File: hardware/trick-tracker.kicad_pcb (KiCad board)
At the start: 4 copper layers, 31 x 45 mm, 58 parts, among them J1 USB4105-GF-A, J2 S2B-PH-K, J3 QWiiC, J4 MEM2061-01-188-00-A, J6 QWiiC, P1 SMTB-1240-S-R, U1 MS88SF2, U2 DPS368XTSA1, U3 LSM9DS1, U4 MCP73831/OT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

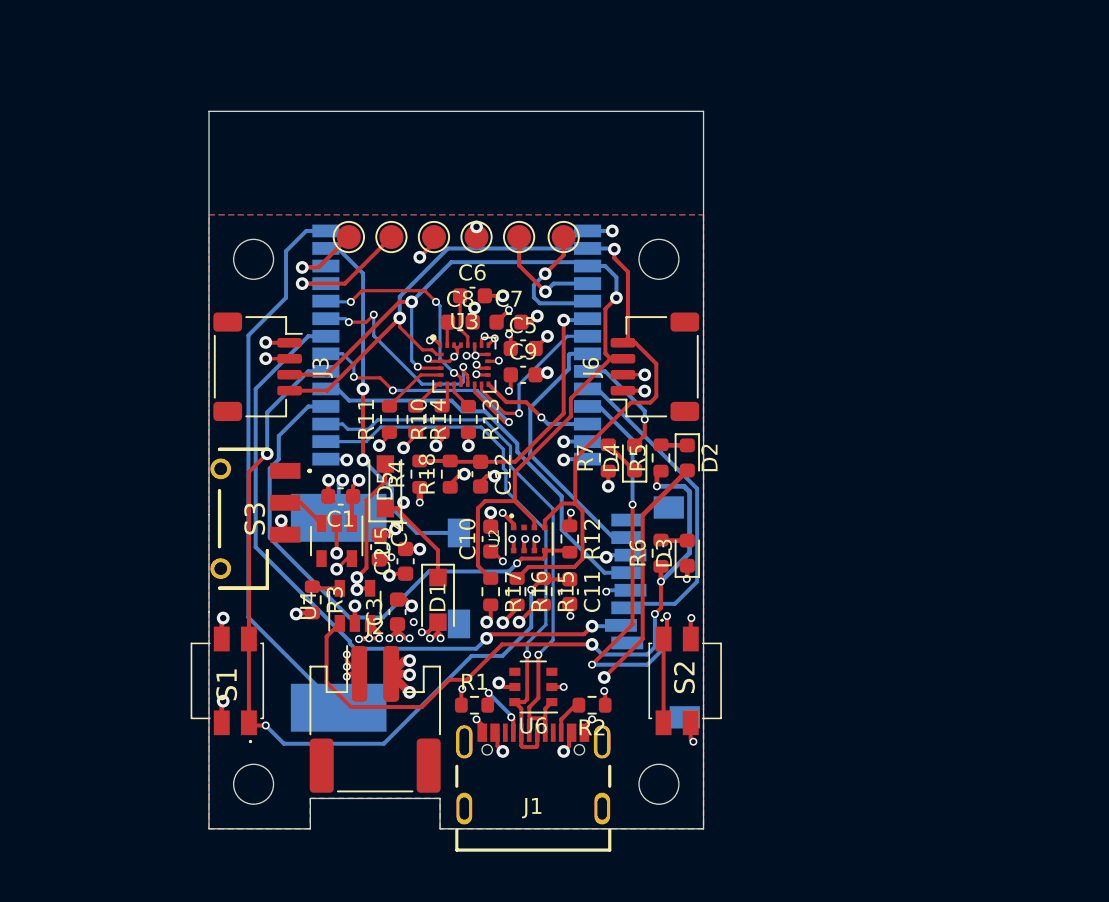
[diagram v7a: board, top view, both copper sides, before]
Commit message: Placed and moved labels
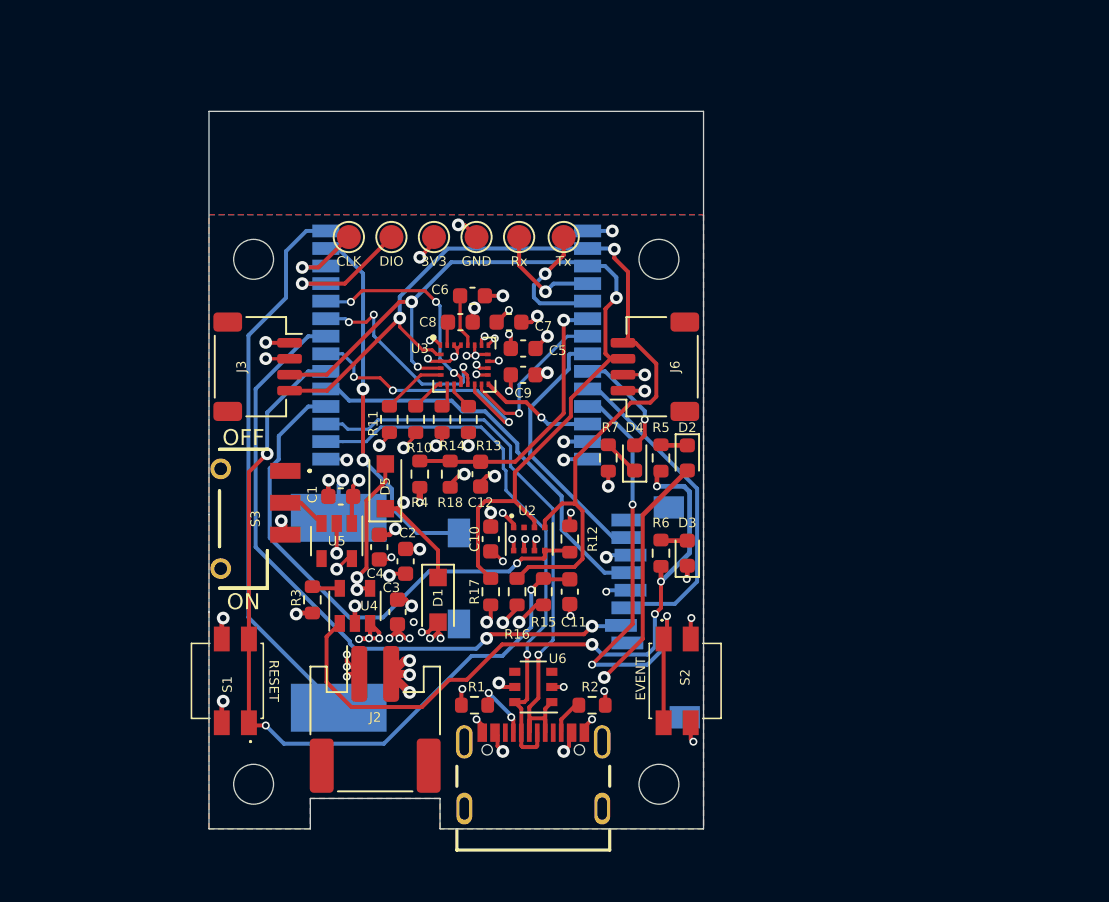
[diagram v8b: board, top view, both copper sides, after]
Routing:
- net GND: track 52.7 -> 53.5 mm
- added copper zone on F.Cu, net GND
- removed copper zone on F.Cu, net (none)
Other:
- board text added: "3V3"
- board text added: "CLK"
- board text added: "DIO"
- board text added: "EVENT"
- board text added: "GND"
- board text added: "OFF"
- board text added: "ON"
- board text added: "RESET"
- board text added: "Rx"
- board text added: "Tx"
